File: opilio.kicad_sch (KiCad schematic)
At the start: 90 parts, among them J1 Screw_Terminal_01x02, J2 USB_C_Receptacle_USB2.0, J3 Conn_01x02_Male, J4 Conn_01x02_Male, J5 Conn_01x02_Male, Q1 PMV25ENEAR, Q2 AO3401A, SW1 Reset, SW2 Boot, U1 EUP3458, U2 STM32F103C8T6, Y1 YSX531SL 8MHz, Y2 YST310S 32.768KHz

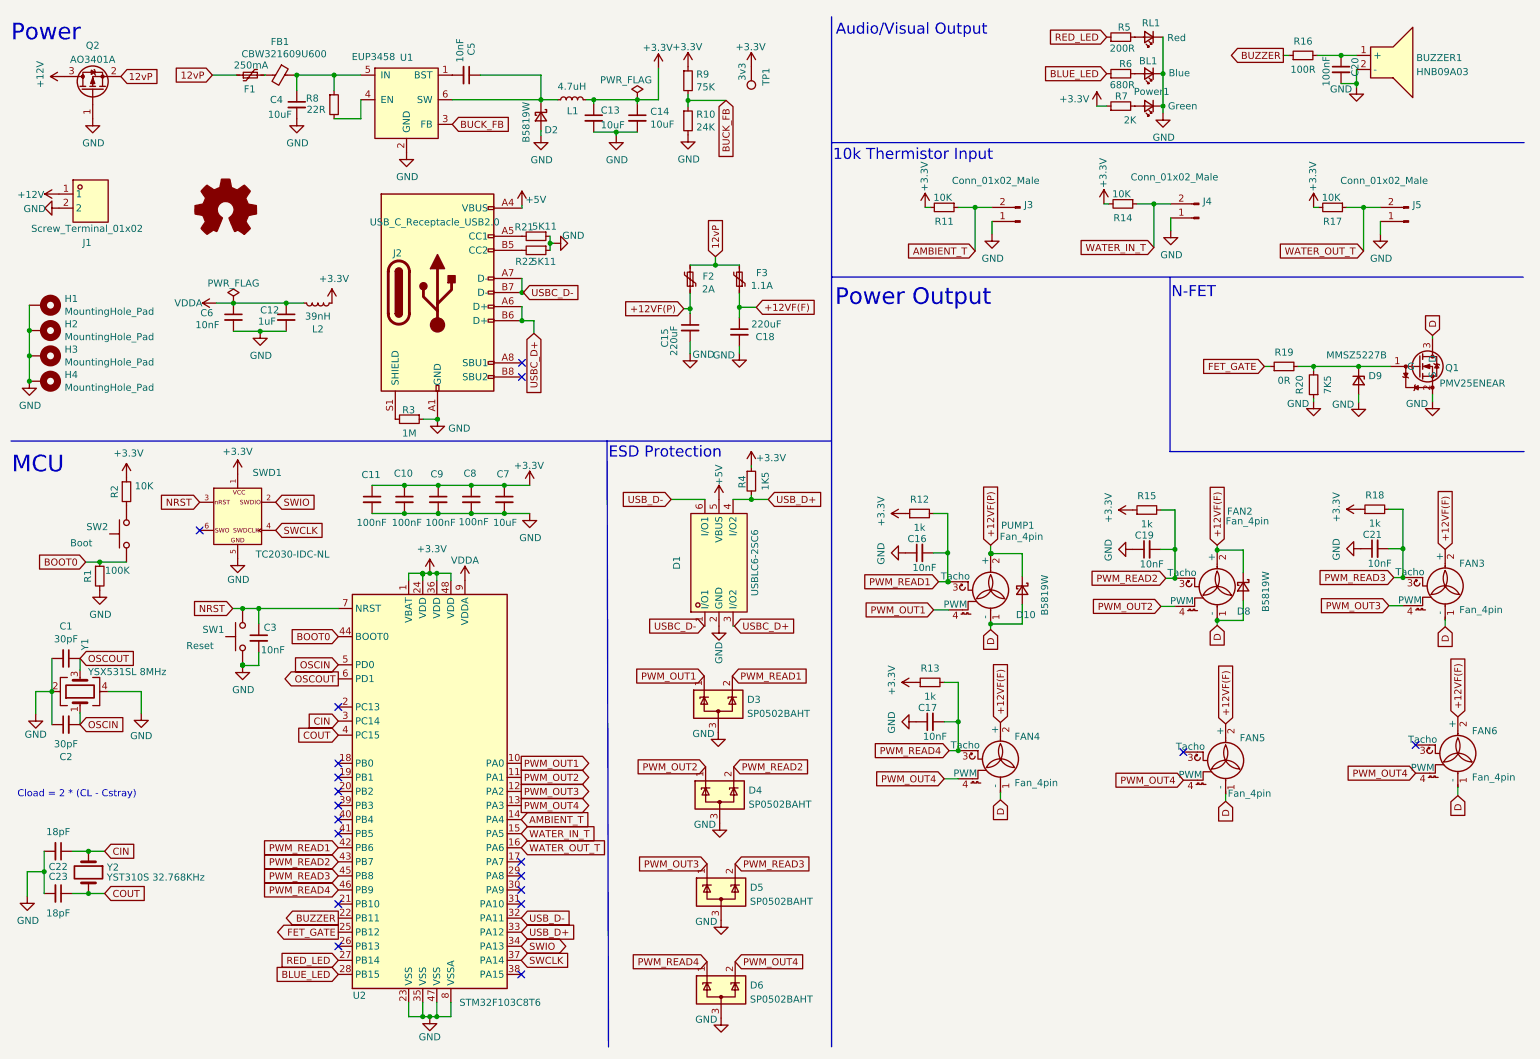
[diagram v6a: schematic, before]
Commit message: v6 with P-channel mosfet
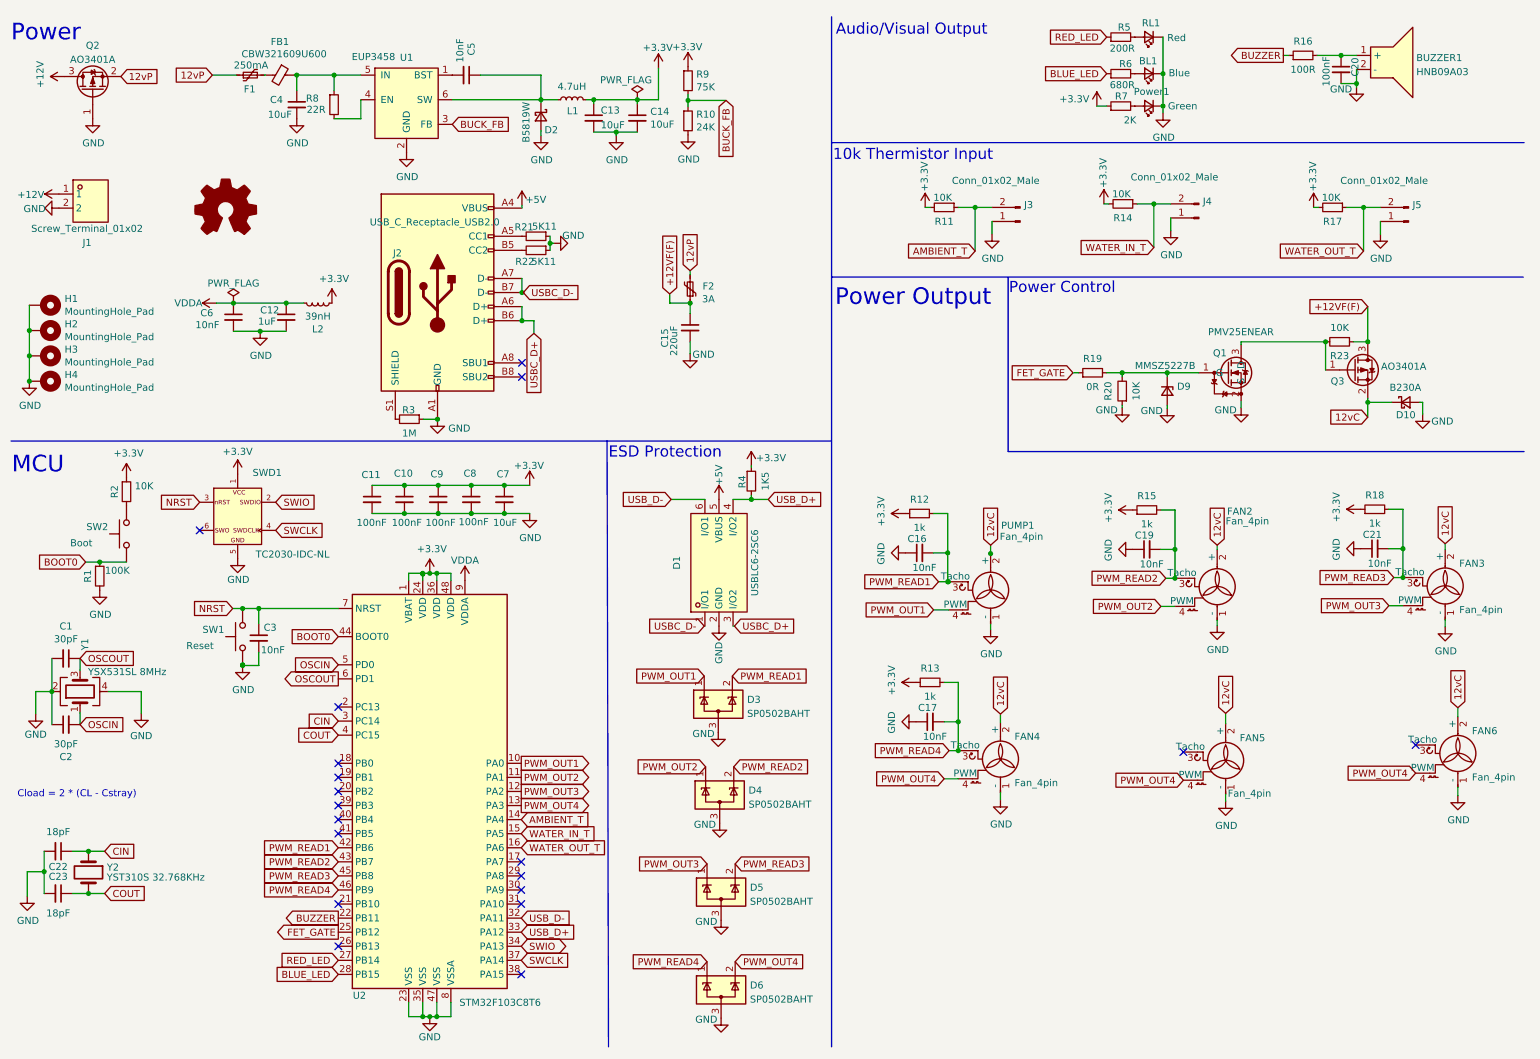
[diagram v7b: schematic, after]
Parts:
- removed C18: 220uF, Capacitor_SMD:CP_Elec_6.3x7.7, symbol Device:C_Small
- removed D8: B5819W, Diode_SMD:D_SMA-SMB_Universal_Handsoldering, symbol Device:D_Schottky_Small
- removed F3: 1.1A, Fuse:Fuse_1206_3216Metric_Pad1.42x1.75mm_HandSolder, symbol Device:Polyfuse_Small
- removed TP1: 3v3, TestPoint:TestPoint_Pad_D1.0mm, symbol Connector:TestPoint
- added Q3: AO3401A, Package_TO_SOT_SMD:SOT-23, symbol Transistor_FET:AO3401A
- added R23: 10K, Resistor_SMD:R_0402_1005Metric_Pad0.72x0.64mm_HandSolder, symbol Device:R_Small
- D10: value B5819W -> B230A; footprint Diode_SMD:D_SMA-SMB_Universal_Handsoldering -> Diode_SMD:D_SMA
- F2: value 2A -> 3A
- R20: value 7K5 -> 10K
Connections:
- net +12VF(F): now also C15.1, F2.1, Q3.3 (D), R23.1; no longer FAN2.2 (+), FAN3.2 (+), FAN4.2 (+), FAN5.2 (+), FAN6.2 (+)
- net GND: now also D10.2 (A), FAN2.1 (-), FAN3.1 (-), FAN4.1 (-), FAN5.1 (-), FAN6.1 (-), PUMP1.1 (-)
- net +12VF(P) renamed 12vC
- net 12vC: now also FAN2.2 (+), FAN3.2 (+), FAN4.2 (+), FAN5.2 (+), FAN6.2 (+), Q3.2 (S); no longer C15.1, F2.1
- removed net D: D10.2 (A), FAN2.1 (-), FAN3.1 (-), FAN4.1 (-), FAN5.1 (-), FAN6.1 (-), PUMP1.1 (-), Q1.3 (D)
- new net: Q1.3 (D), Q3.1 (G), R23.2
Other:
- note added: "Power Control"
- note removed: "N-FET"
- moved on the sheet: D10, D9, F2, Q1, R19, R20

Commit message: With sata pewer connector (#3)
* fix mosfet orientation

* update components

* cleanup

* improve design

* new terminal block

* improvements

* initial routing

* nearly ready

* double mosfets

* move bottom esd diode

* match swd wires with bluepill

* before split schema

* split schema, re-route, horizontal fan connectors

* render

* rev-7 ready
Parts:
- removed BL1: Blue, LED_SMD:LED_0603_1608Metric_Pad1.05x0.95mm_HandSolder, symbol Device:LED_Small
- removed BUZZER1: HNB09A03, easyeda2kicad:BUZ-TH_BD9.0-P5.00-D0.6-FD, symbol easyeda:HNB09A03
- removed C1: 30pF, Capacitor_SMD:C_0402_1005Metric_Pad0.74x0.62mm_HandSolder, symbol Device:C_Small
- removed C12: 1uF, Capacitor_SMD:C_0603_1608Metric_Pad1.08x0.95mm_HandSolder, symbol Device:C_Small
- removed C13, C14, C4: 10uF, Capacitor_SMD:C_0603_1608Metric_Pad1.08x0.95mm_HandSolder, symbol Device:C_Small
- removed C15: 220uF, Capacitor_SMD:CP_Elec_6.3x7.7, symbol Device:C_Small
- removed C16, C17, C19, C21, C5: 10nF, Capacitor_SMD:C_0402_1005Metric_Pad0.74x0.62mm_HandSolder, symbol Device:C_Small
- removed C20: 100nF, Capacitor_SMD:C_0402_1005Metric_Pad0.74x0.62mm_HandSolder, symbol Device:C_Small
- removed D1: USBLC6-2SC6, Package_TO_SOT_SMD:SOT-666, symbol easyeda:USBLC6-2P6_C2827693
- removed D10: B230A, Diode_SMD:D_SMA, symbol Device:D_Schottky_Small
- removed D2: B5819W, Diode_SMD:D_SOD-123, symbol Device:D_Schottky_Small
- removed D3, D4, D5, D6: SP0502BAHT, Package_TO_SOT_SMD:SOT-23, symbol Power_Protection:SP0502BAHT
- removed D9: MMSZ5227B, Diode_SMD:D_SOD-123, symbol Device:D_Zener_Small
- removed F1: 250mA, Fuse:Fuse_1206_3216Metric_Pad1.42x1.75mm_HandSolder, symbol Device:Polyfuse_Small
- removed F2: 3A, Fuse:Fuse_1206_3216Metric_Pad1.42x1.75mm_HandSolder, symbol Device:Polyfuse_Small
- removed FAN2, FAN3, FAN4, FAN5, FAN6, PUMP1: Fan_4pin, Custom:FanPinHeader_1x04_P2.54mm_Vertical_no_hole, symbol Motor:Fan_4pin
- removed FB1: CBW321609U600, Capacitor_SMD:C_1206_3216Metric_Pad1.33x1.80mm_HandSolder, symbol Device:FerriteBead_Small
- removed J1: Screw_Terminal_01x02, TerminalBlock:TerminalBlock_bornier-2_P5.08mm, symbol easyeda:JL300-50002U01
- removed J2: USB_C_Receptacle_USB2.0, Custom:USB_C_Receptacle_Palconn_UTC16-G_Streached_pads, symbol Connector:USB_C_Receptacle_USB2.0
- removed J3, J4, J5: Conn_01x02_Male, Connector_PinHeader_2.54mm:PinHeader_1x02_P2.54mm_Vertical, symbol Connector:Conn_01x02_Male
- removed L1: 4.7uH, Inductor_SMD:L_Bourns-SRN4018, symbol Device:L_Small
- removed L2: 39nH, Inductor_SMD:L_0805_2012Metric_Pad1.05x1.20mm_HandSolder, symbol Device:L_Small
- removed Power1: Green, LED_SMD:LED_0603_1608Metric_Pad1.05x0.95mm_HandSolder, symbol Device:LED_Small
- removed Q1: PMV25ENEAR, Package_TO_SOT_SMD:SOT-23, symbol easyeda:PMV25ENEAR
- removed Q2, Q3: AO3401A, Package_TO_SOT_SMD:SOT-23, symbol Transistor_FET:AO3401A
- removed R10: 24K, Resistor_SMD:R_0402_1005Metric_Pad0.72x0.64mm_HandSolder, symbol Device:R_Small
- removed R11, R14, R17, R2, R20, R23: 10K, Resistor_SMD:R_0402_1005Metric_Pad0.72x0.64mm_HandSolder, symbol Device:R_Small
- removed R12, R13, R15, R18: 1k, Resistor_SMD:R_0402_1005Metric_Pad0.72x0.64mm_HandSolder, symbol Device:R_Small
- removed R16: 100R, Resistor_SMD:R_0402_1005Metric_Pad0.72x0.64mm_HandSolder, symbol Device:R_Small
- removed R19: 0R, Resistor_SMD:R_0402_1005Metric_Pad0.72x0.64mm_HandSolder, symbol Device:R_Small
- removed R21, R22: 5K11, Resistor_SMD:R_0402_1005Metric_Pad0.72x0.64mm_HandSolder, symbol Device:R_Small
- removed R3: 1M, Resistor_SMD:R_0402_1005Metric_Pad0.72x0.64mm_HandSolder, symbol Device:R_Small
- removed R4: 1K5, Resistor_SMD:R_0402_1005Metric_Pad0.72x0.64mm_HandSolder, symbol Device:R_Small
- removed R5: 200R, Resistor_SMD:R_0402_1005Metric_Pad0.72x0.64mm_HandSolder, symbol Device:R_Small
- removed R6: 680R, Resistor_SMD:R_0402_1005Metric_Pad0.72x0.64mm_HandSolder, symbol Device:R_Small
- removed R7: 2K, Resistor_SMD:R_0402_1005Metric_Pad0.72x0.64mm_HandSolder, symbol Device:R_Small
- removed R8: 22R, Resistor_SMD:R_0402_1005Metric_Pad0.72x0.64mm_HandSolder, symbol Device:R_Small
- removed R9: 75K, Resistor_SMD:R_0402_1005Metric_Pad0.72x0.64mm_HandSolder, symbol Device:R_Small
- removed RL1: Red, LED_SMD:LED_0603_1608Metric_Pad1.05x0.95mm_HandSolder, symbol Device:LED_Small
- removed SW1: Reset, easyeda2kicad:SW-SMD_L3.0-W2.5-P3.40-LS4.0-L, symbol Switch:SW_Push
- removed SW2: Boot, easyeda2kicad:SW-SMD_L3.0-W2.5-P3.40-LS4.0-L, symbol Switch:SW_Push
- removed U1: EUP3458, Package_TO_SOT_SMD:SOT-23-6_Handsoldering, symbol Custom:EUP3458
- removed Y1: YSX531SL 8MHz, Crystal:Crystal_SMD_3225-4Pin_3.2x2.5mm, symbol Device:Crystal_GND24
- added C3: 18pF, Capacitor_SMD:C_0402_1005Metric, symbol Device:C_Small
- added J1: Conn_01x04_Male, Connector_PinHeader_2.54mm:PinHeader_1x04_P2.54mm_Vertical, symbol Connector:Conn_01x04_Male
- added SW1, SW2: TS-1077S-01726, easyeda2kicad:KEY-SMD_4P-L3.1-W3.1-P2.00_TS-1077S-01726, symbol easyeda:TS-1077S-01726
- added Y2: TAXM8M4RFDCET2T, easyeda2kicad:OSC-SMD_4P-L3.2-W2.5-BL, symbol easyeda:TAXM8M4RFDCET2T
- C1: renamed from C3; value 10nF -> 100nF; footprint Capacitor_SMD:C_0402_1005Metric_Pad0.74x0.62mm_HandSolder -> Capacitor_SMD:C_0402_1005Metric; LCSC Part C272878 -> C100072
- C10: renamed from C8; footprint Capacitor_SMD:C_0402_1005Metric_Pad0.74x0.62mm_HandSolder -> Capacitor_SMD:C_0402_1005Metric
- C11: renamed from C7; footprint Capacitor_SMD:C_0603_1608Metric_Pad1.08x0.95mm_HandSolder -> Capacitor_SMD:C_0603_1608Metric
- C2: value 30pF -> 100nF; footprint Capacitor_SMD:C_0402_1005Metric_Pad0.74x0.62mm_HandSolder -> Capacitor_SMD:C_0402_1005Metric; LCSC Part C458861 -> C100072
- C4: renamed from C22; footprint Capacitor_SMD:C_0402_1005Metric_Pad0.74x0.62mm_HandSolder -> Capacitor_SMD:C_0402_1005Metric
- C5: renamed from C23; footprint Capacitor_SMD:C_0402_1005Metric_Pad0.74x0.62mm_HandSolder -> Capacitor_SMD:C_0402_1005Metric
- C6: value 10nF -> 18pF; footprint Capacitor_SMD:C_0402_1005Metric_Pad0.74x0.62mm_HandSolder -> Capacitor_SMD:C_0402_1005Metric; LCSC Part C272878 -> C33149
- C7: renamed from C11; footprint Capacitor_SMD:C_0402_1005Metric_Pad0.74x0.62mm_HandSolder -> Capacitor_SMD:C_0402_1005Metric
- C8: renamed from C10; footprint Capacitor_SMD:C_0402_1005Metric_Pad0.74x0.62mm_HandSolder -> Capacitor_SMD:C_0402_1005Metric
- C9: footprint Capacitor_SMD:C_0402_1005Metric_Pad0.74x0.62mm_HandSolder -> Capacitor_SMD:C_0402_1005Metric
- R1: value 100K -> 10K; footprint Resistor_SMD:R_0402_1005Metric_Pad0.72x0.64mm_HandSolder -> Resistor_SMD:R_0402_1005Metric; LCSC Part C144809 -> C191123
- renumbered U2 to U1, Y2 to Y1
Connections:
- net +3.3V: now also J1.1 (Pin_1), SW2.1, SW2.2
- net BOOT0: now also C2.1, SW2.3, SW2.4
- net GND: now also C2.2, C3.1, J1.4 (Pin_4), SW1.3, SW1.4, SW1.5, SW2.5, Y2.2 (GND), Y2.4 (GND); no longer C2.1
- net NRST: now also SW1.1, SW1.2
- net OSCIN: now also C3.2, Y2.1 (OSC1); no longer C2.2
- net OSCOUT: now also C6.1, Y2.3 (OSC2)
- net SWCLK: now also J1.3 (Pin_3)
- net SWIO: now also J1.2 (Pin_2)
- net VDDA: no longer C6.1
- net FAN_EN: now reaches U1.26 (PB13)
- net GREEN_LED: now reaches U1.29 (PA8)
- net FET_GATE renamed PUMP_EN
- no-connect marks 19 -> 13
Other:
- added sheet Power (power.kicad_sch)
- added sheet fan_connectors (fan_connectors.kicad_sch)
- added sheet io (io.kicad_sch)
- note removed: "10k Thermistor Input"
- note removed: "Audio/Visual Output"
- note removed: "ESD Protection"
- note removed: "Power"
- note removed: "Power Control"
- note removed: "Power Output"
- moved on the sheet: C1, C10, C11, C4, C5, C7, C8, C9, R1, SWD1, U1, Y1
